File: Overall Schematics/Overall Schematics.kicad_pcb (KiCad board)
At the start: 2 copper layers, 152.4 x 167.9 mm, 33 parts, among them J1 WattMeter1_Output, J2 WattMeter2_Output, J3 Intel_Buck_Converter_Input, M1 Stepper_Motor_bipolar, M10 Motor_Servo, M11 Stepper_Motor_bipolar, M12 Motor_Servo, M2 Stepper_Motor_bipolar, M3 LinActuator12V, M4 LinActuator12V, M5 LinActuator12V, M6 Motor_DC, M7 Motor_DC, M8 Motor_DC, M9 Motor_DC, U1 Teensy4.1, U10 VNH52019, U11 ServoDriver, U12 36v4SMD, U13 D24V22F5, U2 36v4SMD, U3 36v4SMD, U4 VNH52019, U5 VNH52019, U6 VNH52019, U7 VNH52019, U8 VNH52019, U9 VNH52019

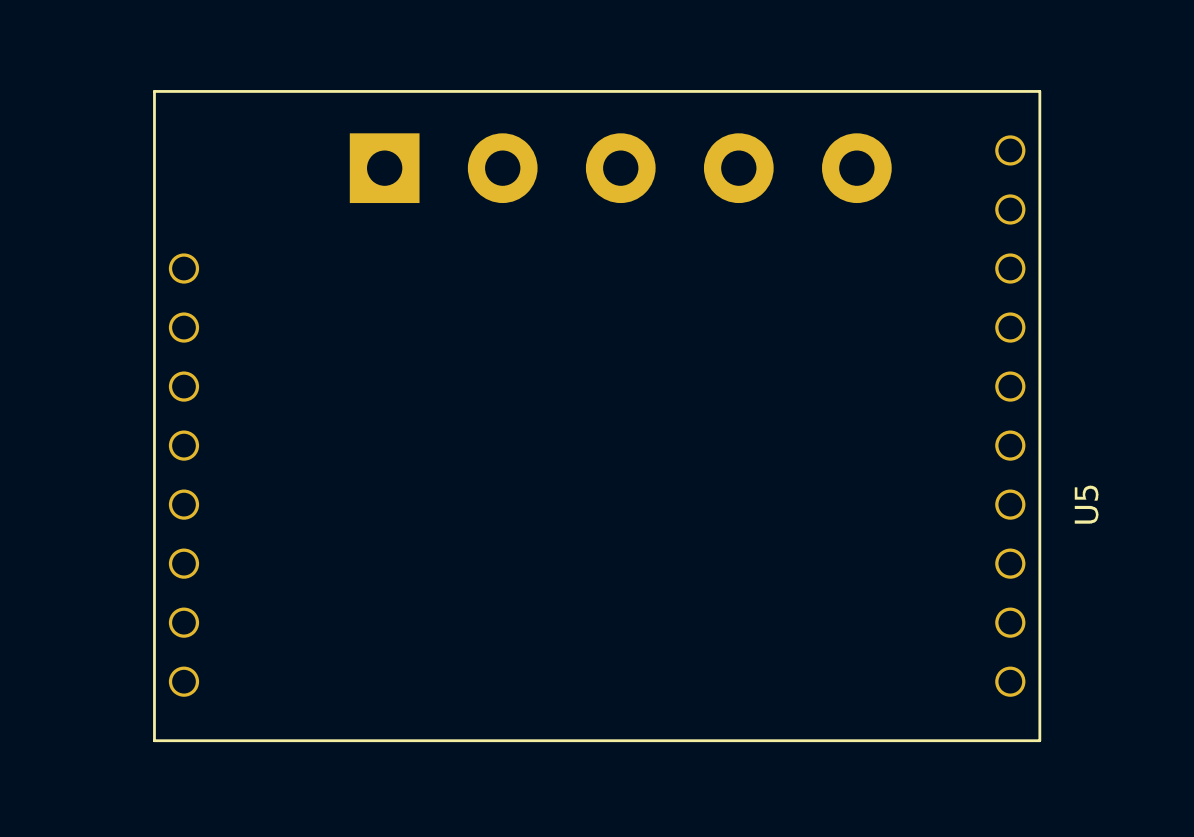
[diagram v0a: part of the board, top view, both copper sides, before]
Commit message: Schematic layout set needs routing
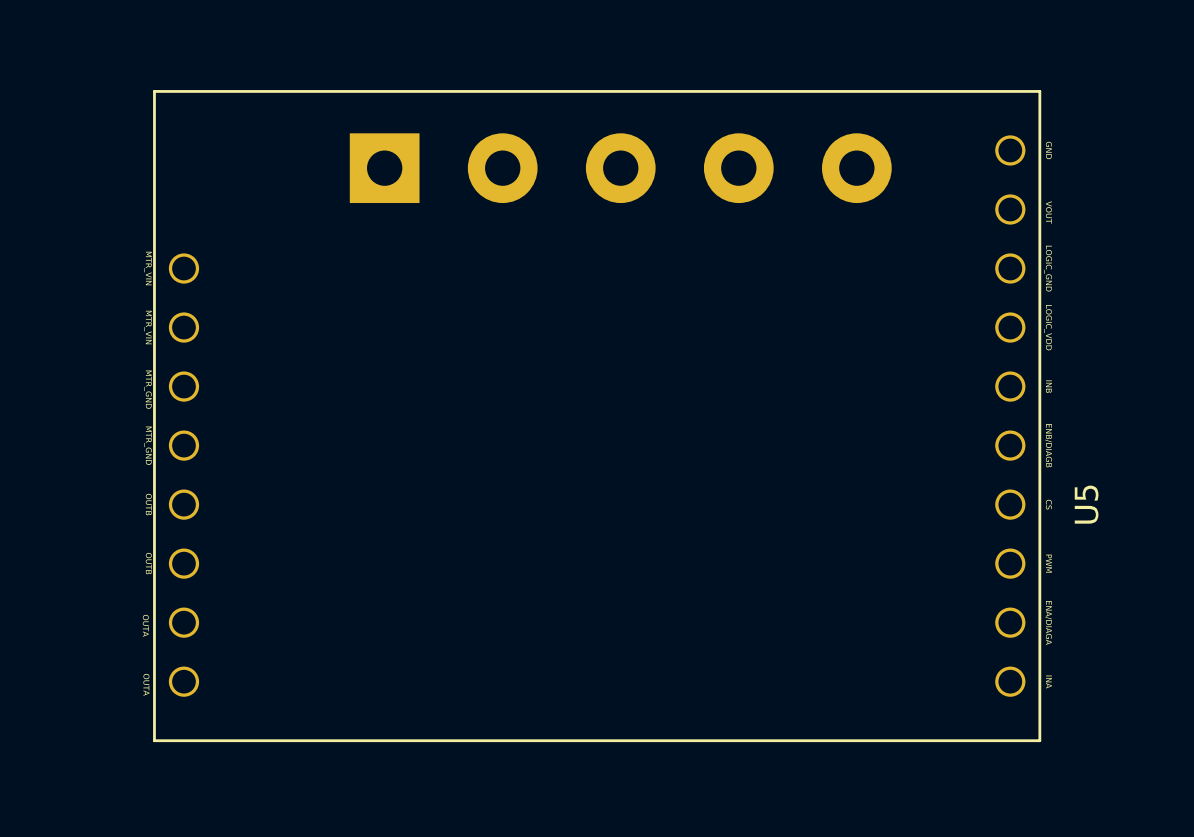
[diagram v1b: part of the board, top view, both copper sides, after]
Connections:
- U1 pad 2: Net-(U1-Pad2) -> unconnected-(U1-Pad2)
- U1 pad 24: Net-(U1-Pad24) -> unconnected-(U1-Pad24)
- U1 pad 25: Net-(U1-Pad25) -> unconnected-(U1-Pad25)
- U1 pad 26: Net-(U1-Pad26) -> unconnected-(U1-Pad26)
- U1 pad 3: Net-(U1-Pad3) -> unconnected-(U1-Pad3)
- U1 pad 33: Net-(U1-Pad33) -> unconnected-(U1-Pad33)
- U1 pad 48: Net-(U1-Pad48) -> unconnected-(U1-Pad48)
- U10 pad 10: Net-(U10-Pad10) -> unconnected-(U10-Pad10)
- U10 pad 11: Battery1_Positive24V -> OUTA_4
- U10 pad 12: PWR_GND -> OUTB_4
- U10 pad 13: OUTB_2 -> PWR_GND
- U10 pad 14: OUTA_1 -> Battery1_Positive24V
- U10 pad 2: Net-(U10-Pad2) -> unconnected-(U10-Pad2)
- U10 pad 4: Net-(U10-Pad4) -> unconnected-(U10-Pad4)
- U10 pad 5: Net-(U10-Pad5) -> unconnected-(U10-Pad5)
- U10 pad 9: Net-(U10-Pad9) -> unconnected-(U10-Pad9)
- U11 pad 10: Net-(U11-Pad10) -> unconnected-(U11-Pad10)
- U11 pad 11: Net-(U11-Pad11) -> unconnected-(U11-Pad11)
- U11 pad 12: Net-(U11-Pad12) -> unconnected-(U11-Pad12)
- U11 pad 15: Net-(U11-Pad15) -> unconnected-(U11-Pad15)
- U11 pad 16: Net-(U11-Pad16) -> unconnected-(U11-Pad16)
- U11 pad 17: Net-(U11-Pad17) -> unconnected-(U11-Pad17)
- U11 pad 18: Net-(U11-Pad18) -> unconnected-(U11-Pad18)
- U11 pad 3: Net-(U11-Pad3) -> unconnected-(U11-Pad3)
- U11 pad 4: Net-(U11-Pad4) -> unconnected-(U11-Pad4)
- U11 pad 5: Net-(U11-Pad5) -> unconnected-(U11-Pad5)
- U11 pad 6: Net-(U11-Pad6) -> unconnected-(U11-Pad6)
- U11 pad 9: Net-(U11-Pad9) -> unconnected-(U11-Pad9)
- U12 pad 1: Net-(U12-Pad1) -> unconnected-(U12-Pad1)
- U12 pad 12: Net-(U12-Pad12) -> unconnected-(U12-Pad12)
- U12 pad 13: Net-(U12-Pad13) -> unconnected-(U12-Pad13)
- U12 pad 14: Net-(U12-Pad14) -> unconnected-(U12-Pad14)
- U12 pad 15: Net-(U12-Pad15) -> unconnected-(U12-Pad15)
- U12 pad 16: Net-(U12-Pad16) -> unconnected-(U12-Pad16)
- U12 pad 2: Net-(U12-Pad2) -> 3.3V
- U12 pad 6: Net-(U12-Pad6) -> unconnected-(U12-Pad6)
- U12 pad 7: Net-(U12-Pad7) -> unconnected-(U12-Pad7)
- U12 pad 8: Net-(U12-Pad8) -> unconnected-(U12-Pad8)
- U12 pad 9: Net-(U12-Pad9) -> unconnected-(U12-Pad9)
- U13 pad 1: Net-(U13-Pad1) -> unconnected-(U13-Pad1)
- U13 pad 2: Net-(U13-Pad2) -> unconnected-(U13-Pad2)
- U2 pad 1: Net-(U2-Pad1) -> unconnected-(U2-Pad1)
- U2 pad 12: Net-(U2-Pad12) -> unconnected-(U2-Pad12)
- U2 pad 13: Net-(U2-Pad13) -> unconnected-(U2-Pad13)
- U2 pad 14: Net-(U2-Pad14) -> unconnected-(U2-Pad14)
- U2 pad 15: Net-(U2-Pad15) -> unconnected-(U2-Pad15)
- U2 pad 16: Net-(U2-Pad16) -> unconnected-(U2-Pad16)
- U2 pad 2: Net-(U2-Pad2) -> 3.3V
- U2 pad 6: Net-(U2-Pad6) -> unconnected-(U2-Pad6)
- U2 pad 7: Net-(U2-Pad7) -> unconnected-(U2-Pad7)
- U2 pad 8: Net-(U2-Pad8) -> unconnected-(U2-Pad8)
- U2 pad 9: Net-(U2-Pad9) -> unconnected-(U2-Pad9)
- U3 pad 1: Net-(U3-Pad1) -> unconnected-(U3-Pad1)
- U3 pad 12: Net-(U3-Pad12) -> unconnected-(U3-Pad12)
- U3 pad 13: Net-(U3-Pad13) -> unconnected-(U3-Pad13)
- U3 pad 14: Net-(U3-Pad14) -> unconnected-(U3-Pad14)
- U3 pad 15: Net-(U3-Pad15) -> unconnected-(U3-Pad15)
- U3 pad 16: Net-(U3-Pad16) -> unconnected-(U3-Pad16)
- U3 pad 2: Net-(U3-Pad2) -> 3.3V
- U3 pad 6: Net-(U3-Pad6) -> unconnected-(U3-Pad6)
- U3 pad 7: Net-(U3-Pad7) -> unconnected-(U3-Pad7)
- U3 pad 8: Net-(U3-Pad8) -> unconnected-(U3-Pad8)
- U3 pad 9: Net-(U3-Pad9) -> unconnected-(U3-Pad9)
- U4 pad 10: Net-(U4-Pad10) -> unconnected-(U4-Pad10)
- U4 pad 11: Battery1_Positive24V -> OUTA2_LIN
- U4 pad 12: PWR_GND -> OUTB2_LIN
- U4 pad 13: OUTB2_LIN -> PWR_GND
- U4 pad 14: OUTA2_LIN -> Battery1_Positive24V
- U4 pad 2: Net-(U4-Pad2) -> unconnected-(U4-Pad2)
- U4 pad 4: Net-(U4-Pad4) -> unconnected-(U4-Pad4)
- U4 pad 5: Net-(U4-Pad5) -> unconnected-(U4-Pad5)
- U4 pad 9: Net-(U4-Pad9) -> unconnected-(U4-Pad9)
- U5 pad 10: Net-(U5-Pad10) -> unconnected-(U5-Pad10)
- U5 pad 2: Net-(U5-Pad2) -> unconnected-(U5-Pad2)
- U5 pad 4: Net-(U5-Pad4) -> unconnected-(U5-Pad4)
- U5 pad 5: Net-(U5-Pad5) -> unconnected-(U5-Pad5)
- U5 pad 9: Net-(U5-Pad9) -> unconnected-(U5-Pad9)
- U6 pad 10: Net-(U6-Pad10) -> unconnected-(U6-Pad10)
- U6 pad 2: Net-(U6-Pad2) -> unconnected-(U6-Pad2)
- U6 pad 4: Net-(U6-Pad4) -> unconnected-(U6-Pad4)
- U6 pad 5: Net-(U6-Pad5) -> unconnected-(U6-Pad5)
- U6 pad 9: Net-(U6-Pad9) -> unconnected-(U6-Pad9)
- U7 pad 10: Net-(U7-Pad10) -> unconnected-(U7-Pad10)
- U7 pad 11: Battery1_Positive24V -> OUTA_1
- U7 pad 12: PWR_GND -> OUTB_1
- U7 pad 13: OUTB_1 -> PWR_GND
- U7 pad 14: OUTA_1 -> Battery1_Positive24V
- U7 pad 2: Net-(U7-Pad2) -> unconnected-(U7-Pad2)
- U7 pad 4: Net-(U7-Pad4) -> unconnected-(U7-Pad4)
- U7 pad 5: Net-(U7-Pad5) -> unconnected-(U7-Pad5)
- U7 pad 9: Net-(U7-Pad9) -> unconnected-(U7-Pad9)
- U8 pad 10: Net-(U8-Pad10) -> unconnected-(U8-Pad10)
- U8 pad 11: Battery1_Positive24V -> OUTA_2
- U8 pad 12: PWR_GND -> OUTB_2
- U8 pad 13: OUTB_2 -> PWR_GND
- U8 pad 14: OUTA_2 -> Battery1_Positive24V
- U8 pad 2: Net-(U8-Pad2) -> unconnected-(U8-Pad2)
- U8 pad 4: Net-(U8-Pad4) -> unconnected-(U8-Pad4)
- U8 pad 5: Net-(U8-Pad5) -> unconnected-(U8-Pad5)
- U8 pad 9: Net-(U8-Pad9) -> unconnected-(U8-Pad9)
- U9 pad 10: Net-(U9-Pad10) -> unconnected-(U9-Pad10)
- U9 pad 2: Net-(U9-Pad2) -> unconnected-(U9-Pad2)
- U9 pad 4: Net-(U9-Pad4) -> unconnected-(U9-Pad4)
- U9 pad 5: Net-(U9-Pad5) -> unconnected-(U9-Pad5)
- U9 pad 9: Net-(U9-Pad9) -> unconnected-(U9-Pad9)

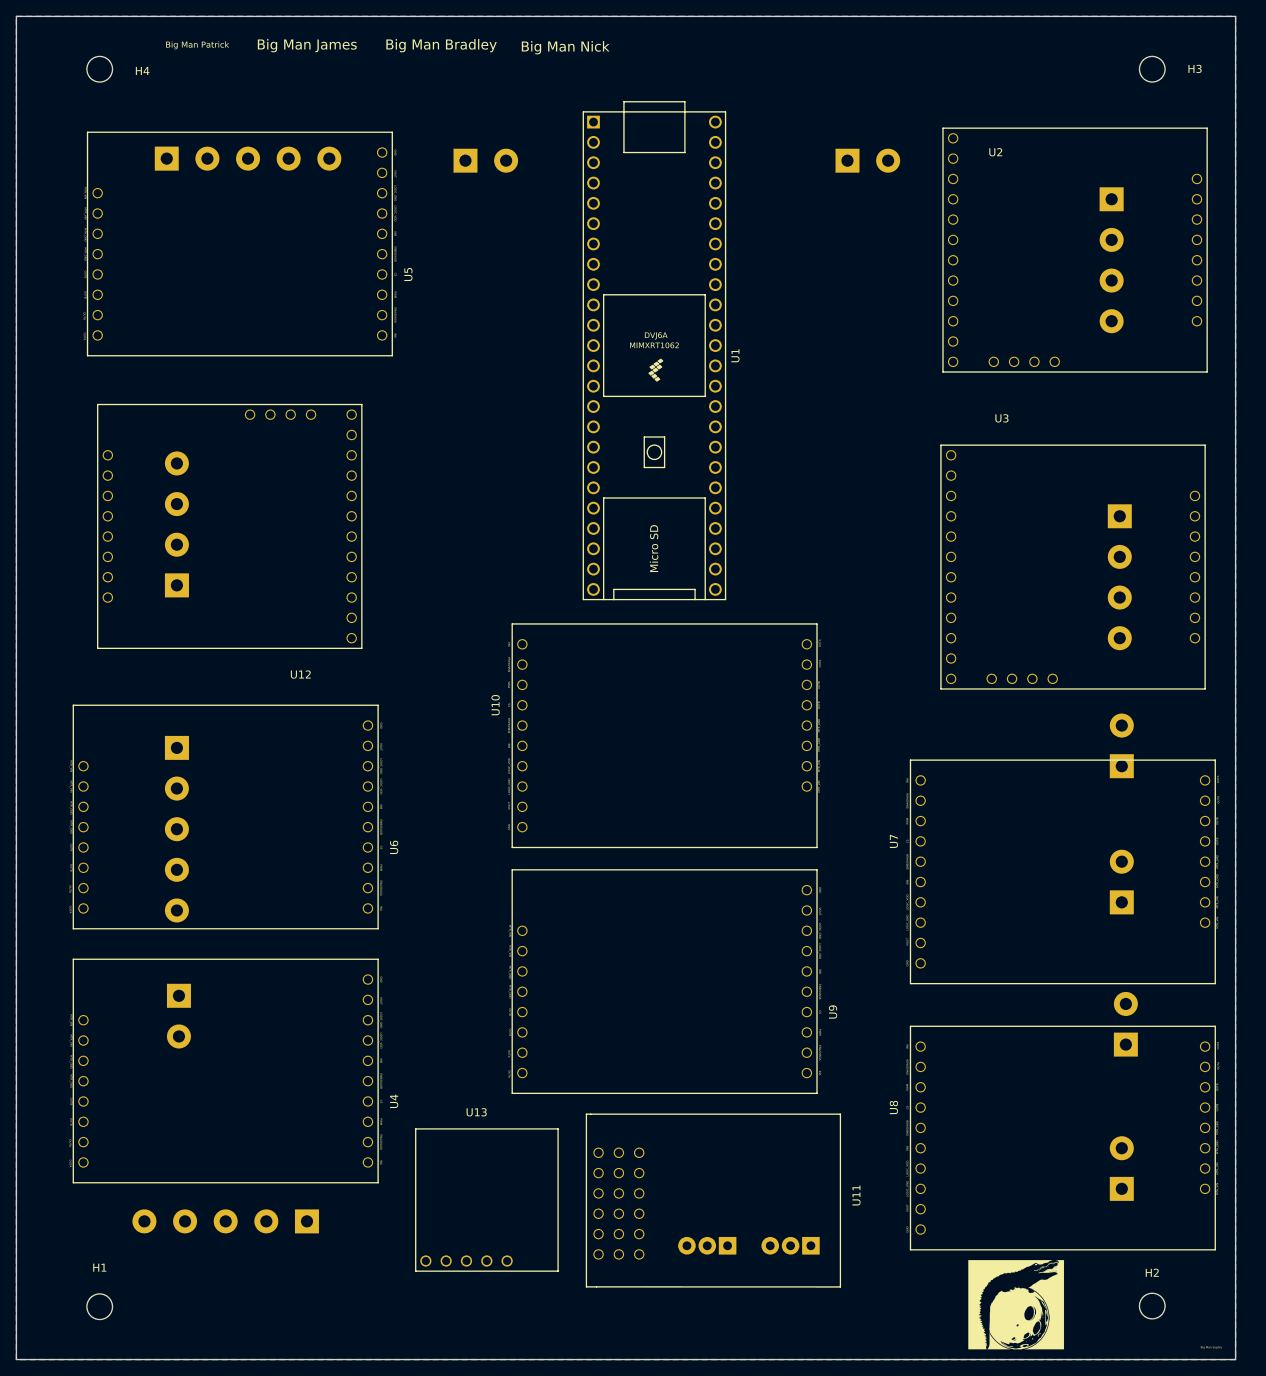
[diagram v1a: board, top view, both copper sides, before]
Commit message: 4-Layer Setup
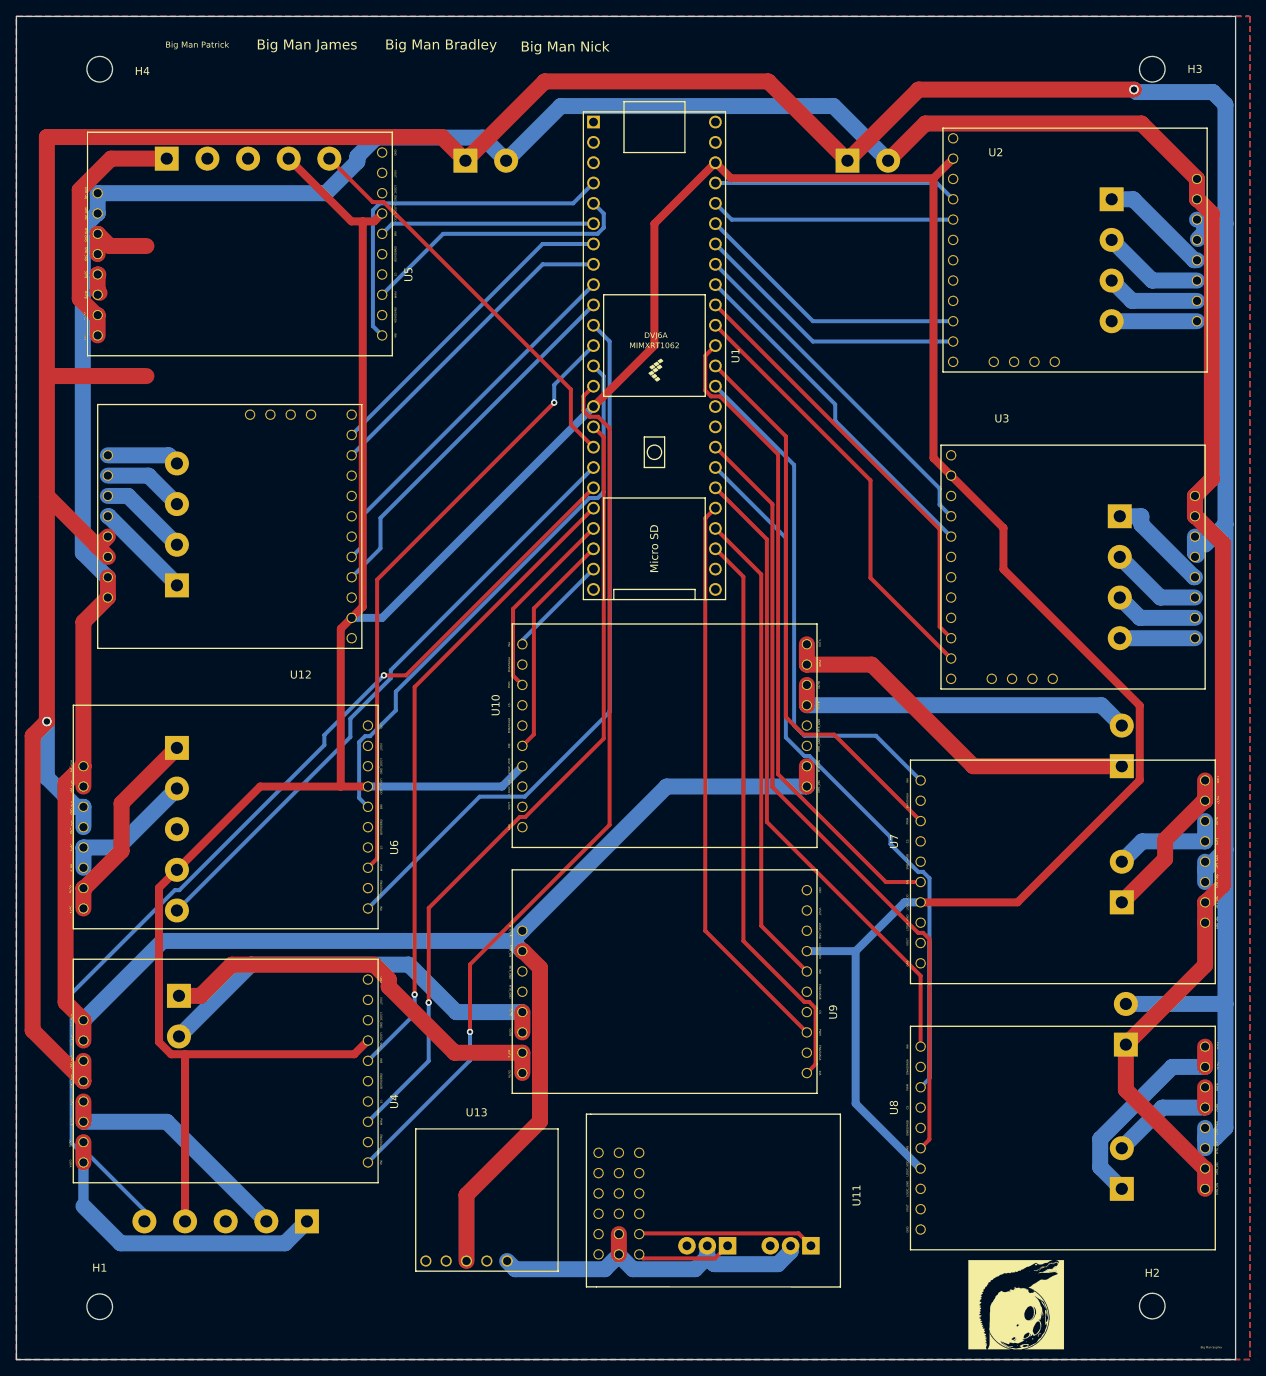
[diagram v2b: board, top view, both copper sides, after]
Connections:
- net PWR_GND renamed Battery_Neg
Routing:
- net Battery1_Positive24V: track 0.00 -> 555.2 mm
- net Battery_Neg: track 0.00 -> 498.5 mm, vias 0 -> 2
- net 3.3V: track 0.00 -> 482.9 mm
- net LIN_SIGNAL2: track 0.00 -> 124.8 mm, vias 0 -> 1
- net INA_6: track 0.00 -> 112.0 mm, vias 0 -> 1
- net PWM_6: track 0.00 -> 100.0 mm, vias 0 -> 1
- net INB_2: track 0.00 -> 99.5 mm
- net PWM_2: track 0.00 -> 89.7 mm
- net INA_5: track 0.00 -> 89.5 mm
- net INB_1: track 0.00 -> 81.9 mm
- net INB_6: track 0.00 -> 80.8 mm, vias 0 -> 1
- net INA_2: track 0.00 -> 80.5 mm
- net PWM_5: track 0.00 -> 77.0 mm, vias 0 -> 1
- net LIN_SIGNAL1: track 0.00 -> 76.9 mm
- net INA_3: track 0.00 -> 71.5 mm
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- added copper zone on B.Cu, net GND
